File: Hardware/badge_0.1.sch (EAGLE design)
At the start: 47 parts, among them CON1 PH_2, IC1 CP2102, SW1 MK12C02, SW2 MK12C02, U4 MCP73832T-2DCI/OT

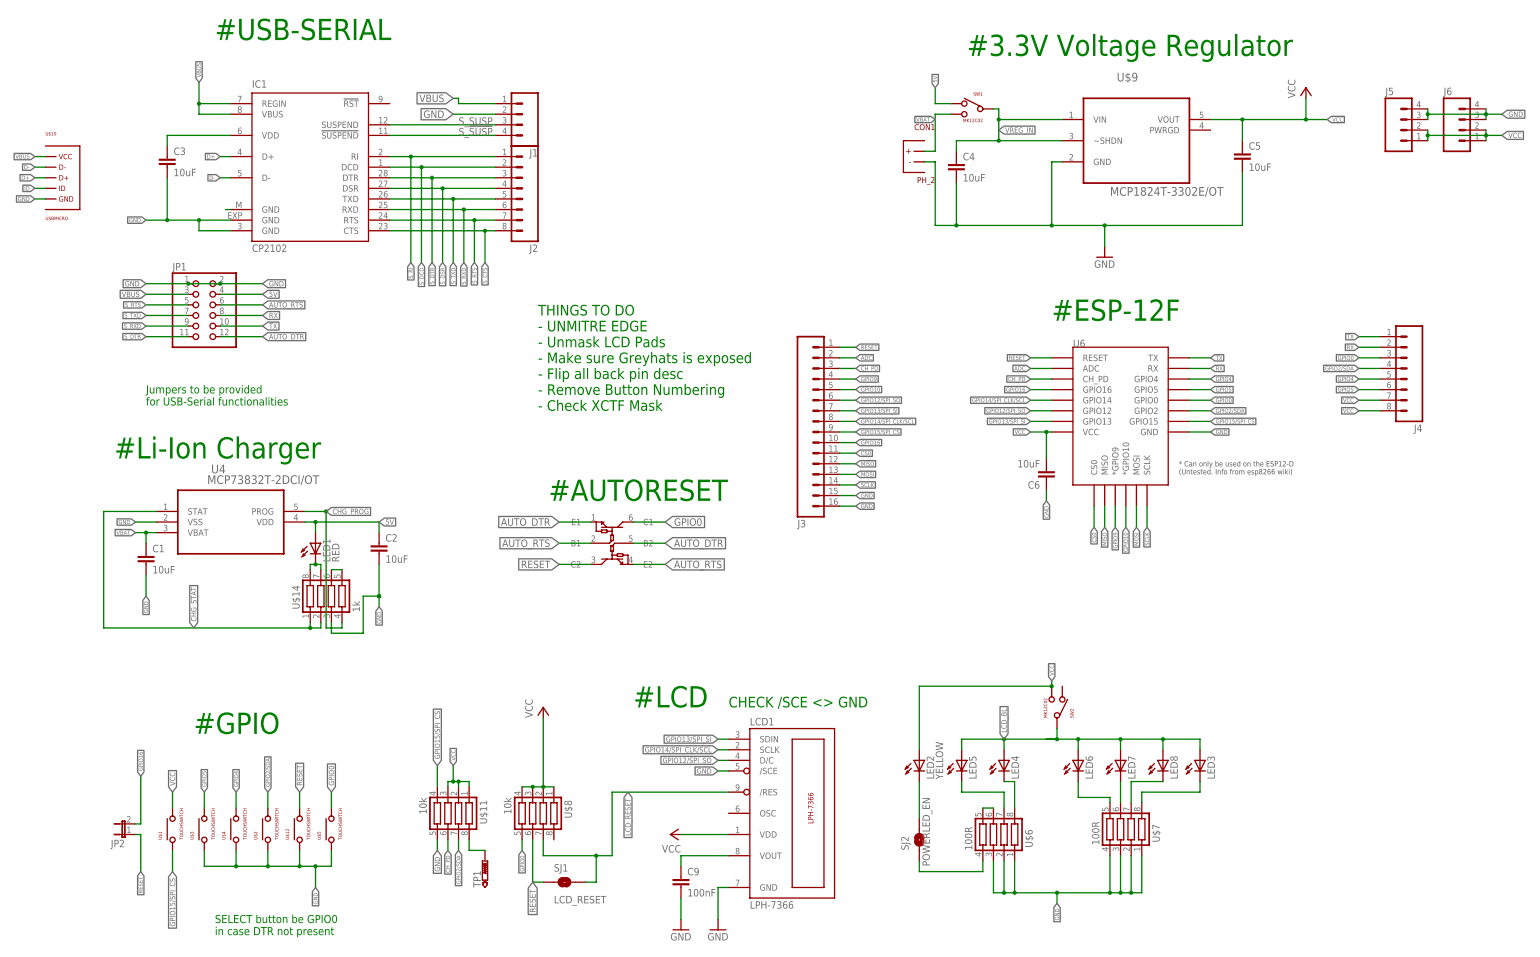
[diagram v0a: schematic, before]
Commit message: updated board schematics and placement
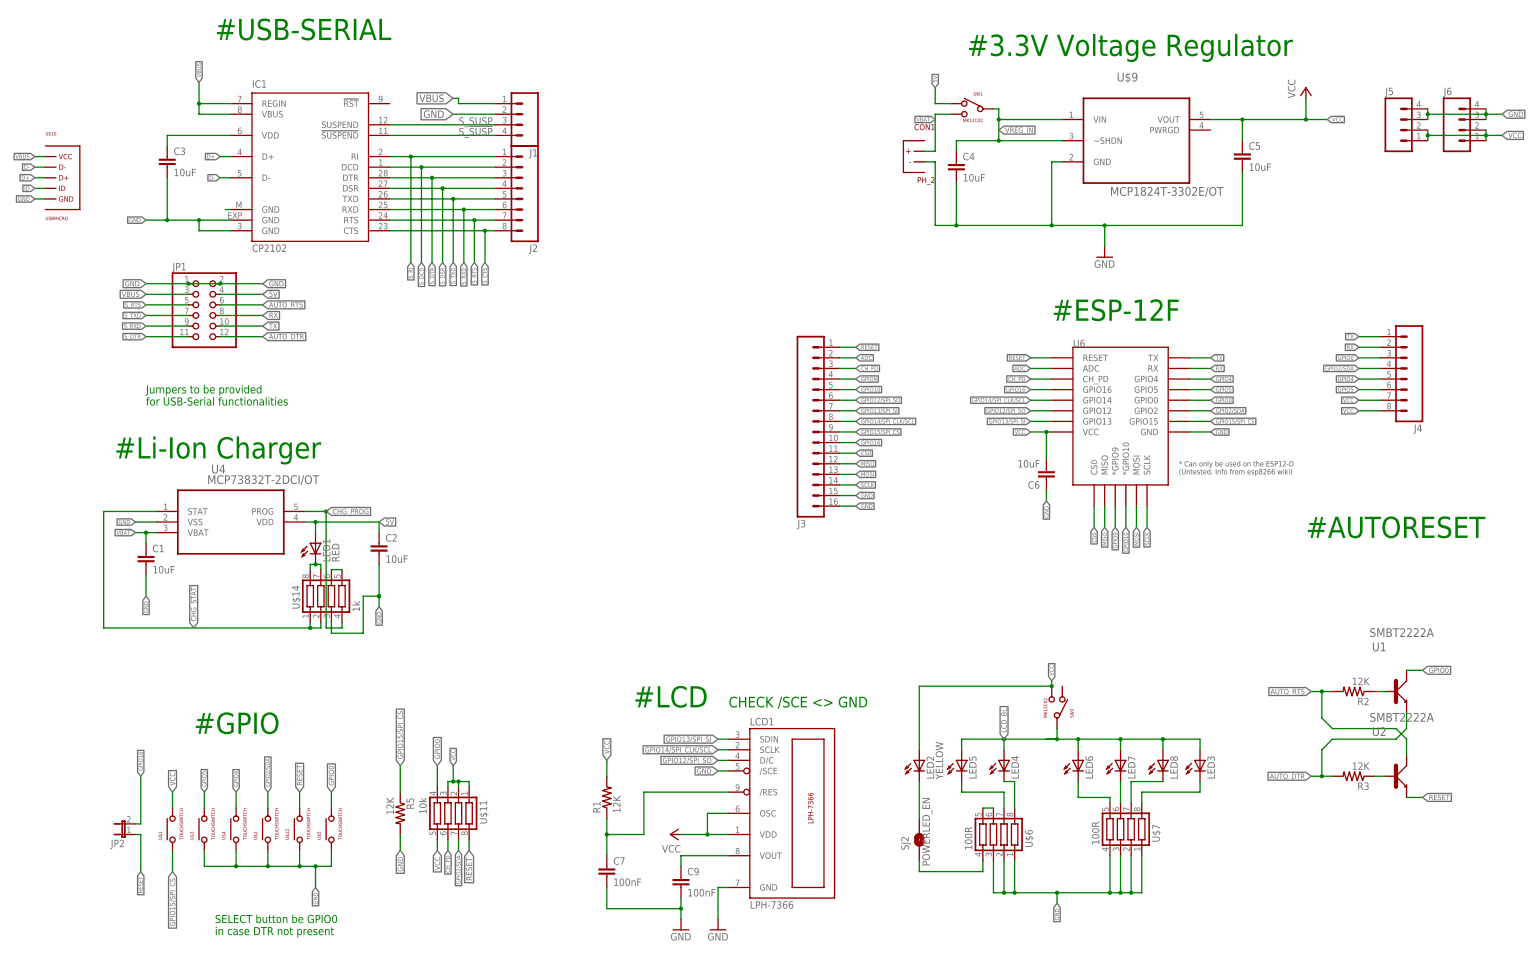
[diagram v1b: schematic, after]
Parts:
- removed SJ1: LCD_RESET, SparkFun-Retired:SOLDERJUMPERTRACE
- removed TP1: PTR1B1,27, testpad:PTR1B1,27
- removed U$13: PEMH9,115, LYS_special:PEMH9,115
- removed U$8: 10k, Simplex-rlc:RES_ARR
- added C7: 100nF, SparkFun-Capacitors:1UF-25V-10%(0805)"
- added R1, R2, R3, R5: 12K, SparkFun-Passives:RESISTOR0805-RES
- added U1, U2: SMBT2222A, badge:SMBT2222A
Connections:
- removed net LCD_RESET: LCD1./RES, SJ1.2, U$8.7
- removed net N$3: TP1.TP, U$11.8
- new net N$10: R2.1, U1.B
- new net N$17: C7.1, LCD1./RES, R1.1
- new net N$18: R3.1, U2.B
- net AUTO_DTR: now also R3.2, U1.E; no longer U$13.B2, U$13.E1
- net AUTO_RTS: now also R2.2, U2.C; no longer U$13.B1, U$13.E2
- net GND: now also C7.2, R5.2; no longer U$11.5
- net GPIO0: now also U$11.4, U1.C; no longer U$13.C1, U$8.5
- net GPIO15/SPI_CS: now also R5.1; no longer U$11.4
- net RESET: now also U$11.8, U2.E; no longer SJ1.1, U$13.C2, U$8.6
- net VCC: now also LCD1.OSC, R1.2, U$11.5; no longer U$8.1, U$8.2, U$8.3, U$8.4
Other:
- note removed: "THINGS TO DO - UNMITRE EDGE - Unmask LCD Pads - Make sure Greyhats is exposed - Flip all back pin desc - Remove Button Numbering - Check XCTF Mask"

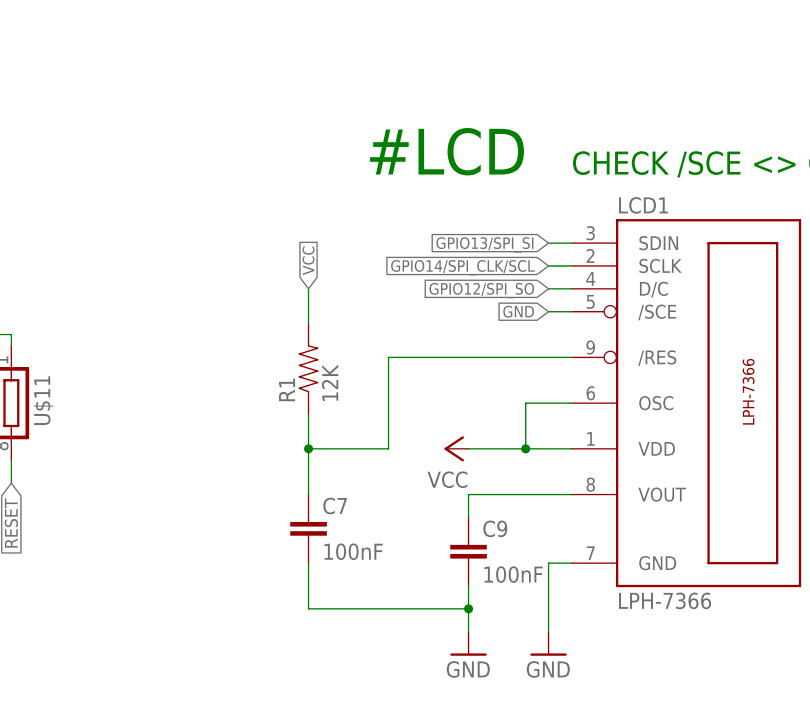
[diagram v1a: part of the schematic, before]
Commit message: added testpoints; converted name into pads
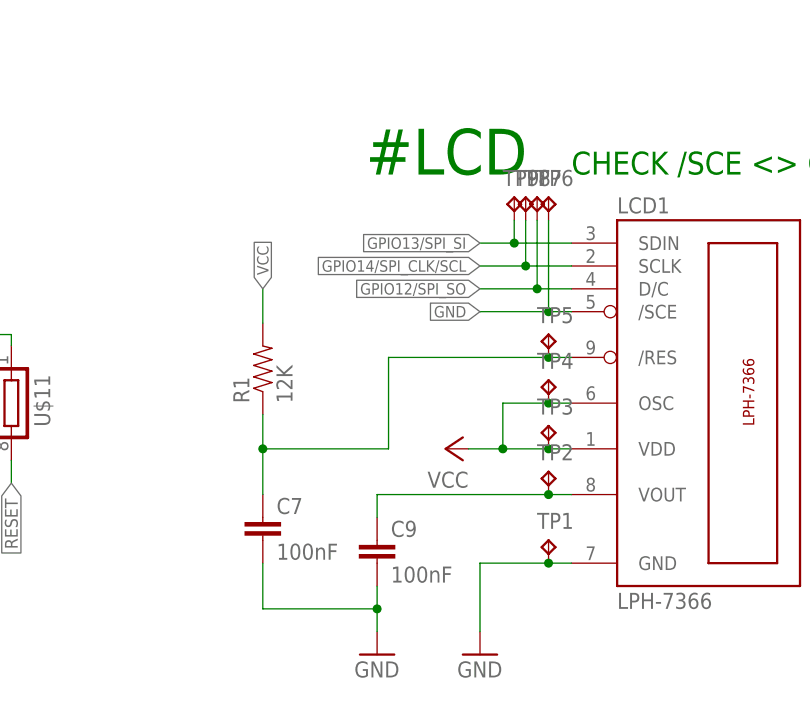
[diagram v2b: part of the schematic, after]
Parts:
- added TP1, TP2, TP3, TP4, TP5, TP6, TP7, TP8, TP9: TPB1,27, testpad:TPB1,27
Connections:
- net GND: now also TP1.TP, TP6.TP
- net GPIO12/SPI_SO: now also TP7.TP
- net GPIO13/SPI_SI: now also TP9.TP
- net GPIO14/SPI_CLK/SCL: now also TP8.TP
- net N$17: now also TP5.TP
- net N$9: now also TP2.TP
- net VCC: now also TP3.TP, TP4.TP
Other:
- moved on the sheet: C7, C9, R1
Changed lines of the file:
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@@
 <part name="R3" library="SparkFun-Passives" deviceset="RESISTOR" device="0805-RES" value="12K"/>
 <part name="R5" library="SparkFun-Passives" deviceset="RESISTOR" device="0805-RES" value="12K"/>
+<part name="TP1" library="testpad" deviceset="TP" device="B1,27" value="TPB1,27"/>
+<part name="TP2" library="testpad" deviceset="TP" device="B1,27" value="TPB1,27"/>
+<part name="TP3" library="testpad" deviceset="TP" device="B1,27" value="TPB1,27"/>
+<part name="TP4" library="testpad" deviceset="TP" device="B1,27" value="TPB1,27"/>
+<part name="TP5" library="testpad" deviceset="TP" device="B1,27" value="TPB1,27"/>
+<part name="TP6" library="testpad" deviceset="TP" device="B1,27" value="TPB1,27"/>
+<part name="TP7" library="testpad" deviceset="TP" device="B1,27" value="TPB1,27"/>
+<part name="TP8" library="testpad" deviceset="TP" device="B1,27" value="TPB1,27"/>
+<part name="TP9" library="testpad" deviceset="TP" device="B1,27" value="TPB1,27"/>
 </parts>
 <sheets>
@@
 <instances>
 <instance part="LCD1" gate="G$1" x="200.66" y="58.42"/>
-<instance part="GND5" gate="1" x="180.34" y="30.48"/>
+<instance part="GND5" gate="1" x="172.72" y="30.48"/>
 <instance part="C4" gate="G$1" x="237.49" y="212.09"/>
 <instance part="C5" gate="G$1" x="306.07" y="214.63"/>
 <instance part="P+5" gate="VCC" x="321.31" y="232.41"/>
 <instance part="GND6" gate="1" x="273.05" y="191.77"/>
-<instance part="C9" gate="G$1" x="171.45" y="40.64"/>
+<instance part="C9" gate="G$1" x="161.29" y="40.64"/>
 <instance part="P+7" gate="VCC" x="168.91" y="53.34" rot="R90"/>
-<instance part="GND10" gate="1" x="171.45" y="30.48"/>
+<instance part="GND10" gate="1" x="161.29" y="30.48"/>
 <instance part="U$1" gate="G$1" x="49.53" y="54.61" rot="R90"/>
 <instance part="U$2" gate="G$1" x="72.39" y="54.61" rot="R90"/>
@@
 <instance part="J6" gate="G$1" x="359.41" y="222.25"/>
 <instance part="C6" gate="G$1" x="259.08" y="140.97" rot="R180"/>
-<instance part="C7" gate="G$1" x="153.67" y="43.18"/>
-<instance part="R1" gate="G$1" x="153.67" y="62.23" rot="R90"/>
+<instance part="C7" gate="G$1" x="148.59" y="43.18"/>
+<instance part="R1" gate="G$1" x="148.59" y="62.23" rot="R90"/>
 <instance part="U1" gate="A" x="342.9" y="87.63"/>
 <instance part="U2" gate="A" x="342.9" y="67.31"/>
@@
 <instance part="R3" gate="G$1" x="332.74" y="67.31" rot="R180"/>
 <instance part="R5" gate="G$1" x="104.14" y="58.42" rot="R270"/>
+<instance part="TP1" gate="G$1" x="180.34" y="43.18"/>
+<instance part="TP2" gate="G$1" x="180.34" y="50.8"/>
+<instance part="TP3" gate="G$1" x="180.34" y="55.88"/>
+<instance part="TP4" gate="G$1" x="180.34" y="60.96"/>
+<instance part="TP5" gate="G$1" x="180.34" y="66.04"/>
+<instance part="TP6" gate="G$1" x="180.34" y="81.28"/>
+<instance part="TP7" gate="G$1" x="179.07" y="81.28"/>
+<instance part="TP8" gate="G$1" x="177.8" y="81.28"/>
+<instance part="TP9" gate="G$1" x="176.53" y="81.28"/>
 </instances>
 <busses>
@@
 <pinref part="P+7" gate="VCC" pin="VCC"/>
 <pinref part="LCD1" gate="G$1" pin="VDD"/>
-<wire x1="171.45" y1="53.34" x2="177.8" y2="53.34" width="0.1524" layer="91"/>
+<wire x1="171.45" y1="53.34" x2="175.26" y2="53.34" width="0.1524" layer="91"/>
 <pinref part="LCD1" gate="G$1" pin="OSC"/>
-<wire x1="177.8" y1="53.34" x2="182.88" y2="53.34" width="0.1524" layer="91"/>
-<wire x1="182.88" y1="58.42" x2="177.8" y2="58.42" width="0.1524" layer="91"/>
-<wire x1="177.8" y1="58.42" x2="177.8" y2="53.34" width="0.1524" layer="91"/>
-<junction x="177.8" y="53.34"/>
+<wire x1="175.26" y1="53.34" x2="180.34" y2="53.34" width="0.1524" layer="91"/>
+<wire x1="180.34" y1="53.34" x2="182.88" y2="53.34" width="0.1524" layer="91"/>
+<wire x1="182.88" y1="58.42" x2="180.34" y2="58.42" width="0.1524" layer="91"/>
+<wire x1="180.34" y1="58.42" x2="175.26" y2="58.42" width="0.1524" layer="91"/>
+<wire x1="175.26" y1="58.42" x2="175.26" y2="53.34" width="0.1524" layer="91"/>
+<junction x="175.26" y="53.34"/>
+<pinref part="TP3" gate="G$1" pin="TP"/>
+<junction x="180.34" y="53.34"/>
+<pinref part="TP4" gate="G$1" pin="TP"/>
+<junction x="180.34" y="58.42"/>
 </segment>
 <segment>
@@
 <segment>
 <pinref part="R1" gate="G$1" pin="2"/>
-<wire x1="153.67" y1="71.12" x2="153.67" y2="67.31" width="0.1524" layer="91"/>
-<label x="153.67" y="71.12" size="1.27" layer="95" rot="R90" xref="yes"/>
+<wire x1="148.59" y1="71.12" x2="148.59" y2="67.31" width="0.1524" layer="91"/>
+<label x="148.59" y="71.12" size="1.27" layer="95" rot="R90" xref="yes"/>
 </segment>
 <segment>
@@
 <pinref part="GND5" gate="1" pin="GND"/>
 <wire x1="182.88" y1="40.64" x2="180.34" y2="40.64" width="0.1524" layer="91"/>
-<wire x1="180.34" y1="40.64" x2="180.34" y2="33.02" width="0.1524" layer="91"/>
+<wire x1="180.34" y1="40.64" x2="172.72" y2="40.64" width="0.1524" layer="91"/>
+<wire x1="172.72" y1="40.64" x2="172.72" y2="33.02" width="0.1524" layer="91"/>
+<pinref part="TP1" gate="G$1" pin="TP"/>
+<junction x="180.34" y="40.64"/>
 </segment>
 <segment>
@@
 <pinref part="GND10" gate="1" pin="GND"/>
 <pinref part="C9" gate="G$1" pin="2"/>
-<wire x1="171.45" y1="38.1" x2="171.45" y2="35.56" width="0.1524" layer="91"/>
+<wire x1="161.29" y1="38.1" x2="161.29" y2="35.56" width="0.1524" layer="91"/>
 <pinref part="C7" gate="G$1" pin="2"/>
-<wire x1="171.45" y1="35.56" x2="171.45" y2="33.02" width="0.1524" layer="91"/>
-<wire x1="153.67" y1="40.64" x2="153.67" y2="35.56" width="0.1524" layer="91"/>
-<wire x1="153.67" y1="35.56" x2="171.45" y2="35.56" width="0.1524" layer="91"/>
-<junction x="171.45" y="35.56"/>
+<wire x1="161.29" y1="35.56" x2="161.29" y2="33.02" width="0.1524" layer="91"/>
+<wire x1="148.59" y1="40.64" x2="148.59" y2="35.56" width="0.1524" layer="91"/>
+<wire x1="148.59" y1="35.56" x2="161.29" y2="35.56" width="0.1524" layer="91"/>
+<junction x="161.29" y="35.56"/>
 </segment>
 <segment>
@@
 <pinref part="LCD1" gate="G$1" pin="/SCE"/>
 <wire x1="182.88" y1="68.58" x2="180.34" y2="68.58" width="0.1524" layer="91"/>
-<label x="180.34" y="68.58" size="1.27" layer="95" rot="R180" xref="yes"/>
+<label x="172.72" y="68.58" size="1.27" layer="95" rot="R180" xref="yes"/>
+<pinref part="TP6" gate="G$1" pin="TP"/>
+<wire x1="180.34" y1="68.58" x2="172.72" y2="68.58" width="0.1524" layer="91"/>
+<wire x1="180.34" y1="78.74" x2="180.34" y2="68.58" width="0.1524" layer="91"/>
+<junction x="180.34" y="68.58"/>
 </segment>
 </net>
@@
 <segment>
 <pinref part="LCD1" gate="G$1" pin="D/C"/>
-<wire x1="182.88" y1="71.12" x2="180.34" y2="71.12" width="0.1524" layer="91"/>
-<label x="180.34" y="71.12" size="1.27" layer="95" rot="MR0" xref="yes"/>
+<wire x1="182.88" y1="71.12" x2="179.07" y2="71.12" width="0.1524" layer="91"/>
+<label x="172.72" y="71.12" size="1.27" layer="95" rot="MR0" xref="yes"/>
+<pinref part="TP7" gate="G$1" pin="TP"/>
+<wire x1="179.07" y1="71.12" x2="172.72" y2="71.12" width="0.1524" layer="91"/>
+<wire x1="179.07" y1="78.74" x2="179.07" y2="71.12" width="0.1524" layer="91"/>
+<junction x="179.07" y="71.12"/>
 </segment>
 <segment>
@@
 <segment>
 <pinref part="LCD1" gate="G$1" pin="SDIN"/>
-<wire x1="182.88" y1="76.2" x2="180.34" y2="76.2" width="0.1524" layer="91"/>
-<label x="180.34" y="76.2" size="1.27" layer="95" rot="MR0" xref="yes"/>
+<wire x1="182.88" y1="76.2" x2="176.53" y2="76.2" width="0.1524" layer="91"/>
+<label x="172.72" y="76.2" size="1.27" layer="95" rot="MR0" xref="yes"/>
+<pinref part="TP9" gate="G$1" pin="TP"/>
+<wire x1="176.53" y1="76.2" x2="172.72" y2="76.2" width="0.1524" layer="91"/>
+<wire x1="176.53" y1="78.74" x2="176.53" y2="76.2" width="0.1524" layer="91"/>
+<junction x="176.53" y="76.2"/>
 </segment>
 <segment>
@@
 <segment>
 <pinref part="LCD1" gate="G$1" pin="SCLK"/>
-<wire x1="182.88" y1="73.66" x2="180.34" y2="73.66" width="0.1524" layer="91"/>
-<label x="180.34" y="73.66" size="1.27" layer="95" rot="MR0" xref="yes"/>
+<wire x1="182.88" y1="73.66" x2="177.8" y2="73.66" width="0.1524" layer="91"/>
+<label x="172.72" y="73.66" size="1.27" layer="95" rot="MR0" xref="yes"/>
+<pinref part="TP8" gate="G$1" pin="TP"/>
+<wire x1="177.8" y1="73.66" x2="172.72" y2="73.66" width="0.1524" layer="91"/>
+<wire x1="177.8" y1="78.74" x2="177.8" y2="73.66" width="0.1524" layer="91"/>
+<junction x="177.8" y="73.66"/>
 </segment>
 <segment>
@@
 <segment>
 <pinref part="C9" gate="G$1" pin="1"/>
-<wire x1="171.45" y1="45.72" x2="171.45" y2="48.26" width="0.1524" layer="91"/>
+<wire x1="161.29" y1="45.72" x2="161.29" y2="48.26" width="0.1524" layer="91"/>
 <pinref part="LCD1" gate="G$1" pin="VOUT"/>
-<wire x1="171.45" y1="48.26" x2="182.88" y2="48.26" width="0.1524" layer="91"/>
+<wire x1="161.29" y1="48.26" x2="180.34" y2="48.26" width="0.1524" layer="91"/>
+<pinref part="TP2" gate="G$1" pin="TP"/>
+<wire x1="180.34" y1="48.26" x2="182.88" y2="48.26" width="0.1524" layer="91"/>
+<junction x="180.34" y="48.26"/>
 </segment>
 </net>
@@
 <pinref part="R1" gate="G$1" pin="1"/>
 <pinref part="C7" gate="G$1" pin="1"/>
-<wire x1="153.67" y1="57.15" x2="153.67" y2="53.34" width="0.1524" layer="91"/>
-<wire x1="153.67" y1="53.34" x2="153.67" y2="48.26" width="0.1524" layer="91"/>
-<wire x1="153.67" y1="53.34" x2="162.56" y2="53.34" width="0.1524" layer="91"/>
+<wire x1="148.59" y1="57.15" x2="148.59" y2="53.34" width="0.1524" layer="91"/>
+<wire x1="148.59" y1="53.34" x2="148.59" y2="48.26" width="0.1524" layer="91"/>
+<wire x1="148.59" y1="53.34" x2="162.56" y2="53.34" width="0.1524" layer="91"/>
 <wire x1="162.56" y1="53.34" x2="162.56" y2="63.5" width="0.1524" layer="91"/>
-<junction x="153.67" y="53.34"/>
+<junction x="148.59" y="53.34"/>
 <pinref part="LCD1" gate="G$1" pin="/RES"/>
-<wire x1="182.88" y1="63.5" x2="162.56" y2="63.5" width="0.1524" layer="91"/>
-</segment>
-</net>
+<wire x1="182.88" y1="63.5" x2="180.34" y2="63.5" width="0.1524" layer="91"/>
+<pinref part="TP5" gate="G$1" pin="TP"/>
+<wire x1="180.34" y1="63.5" x2="162.56" y2="63.5" width="0.1524" layer="91"/>
+<junction x="180.34" y="63.5"/>
+</segment>
+</net>
